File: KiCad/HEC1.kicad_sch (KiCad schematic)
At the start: 9 parts, among them J1 Barrel_Jack_Switch

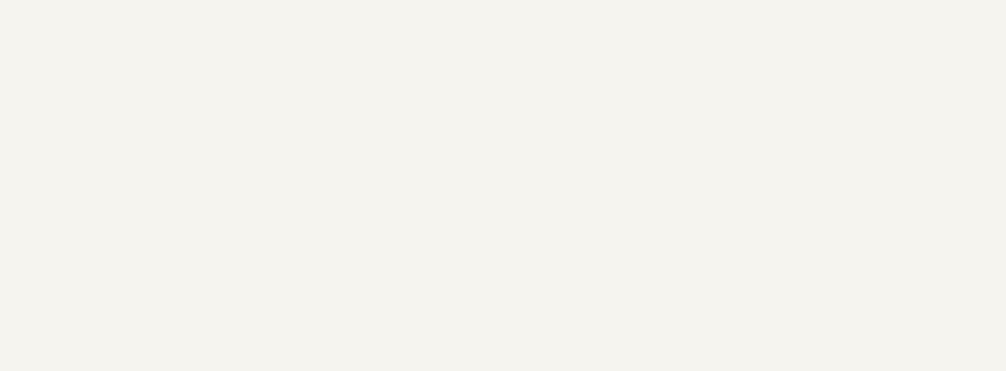
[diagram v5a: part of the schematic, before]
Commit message: MATX-compliant motherboard
Made the motherboard mounting holes and card positions MATX compliant. The MATX motherboard edge is shifted 0.5 inches to the left, which is annoying. Also, cards have component on the opposite side from ISA, meaning PCI slot positioning must be followed. However, PCI pins are not 0.1inch apart, so lining up is tricky. I don't know whether I got it right.
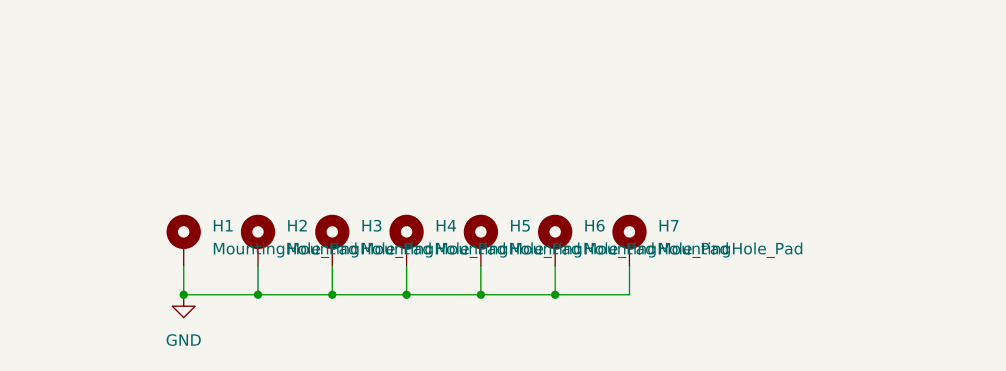
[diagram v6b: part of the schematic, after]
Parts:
- added H1, H2, H3, H4, H5, H6, H7: MountingHole_Pad, MountingHole:MountingHole_3.2mm_M3_Pad_Via, symbol Mechanical:MountingHole_Pad
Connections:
- net GND: now also H1.1, H2.1, H3.1, H4.1, H5.1, H6.1, H7.1

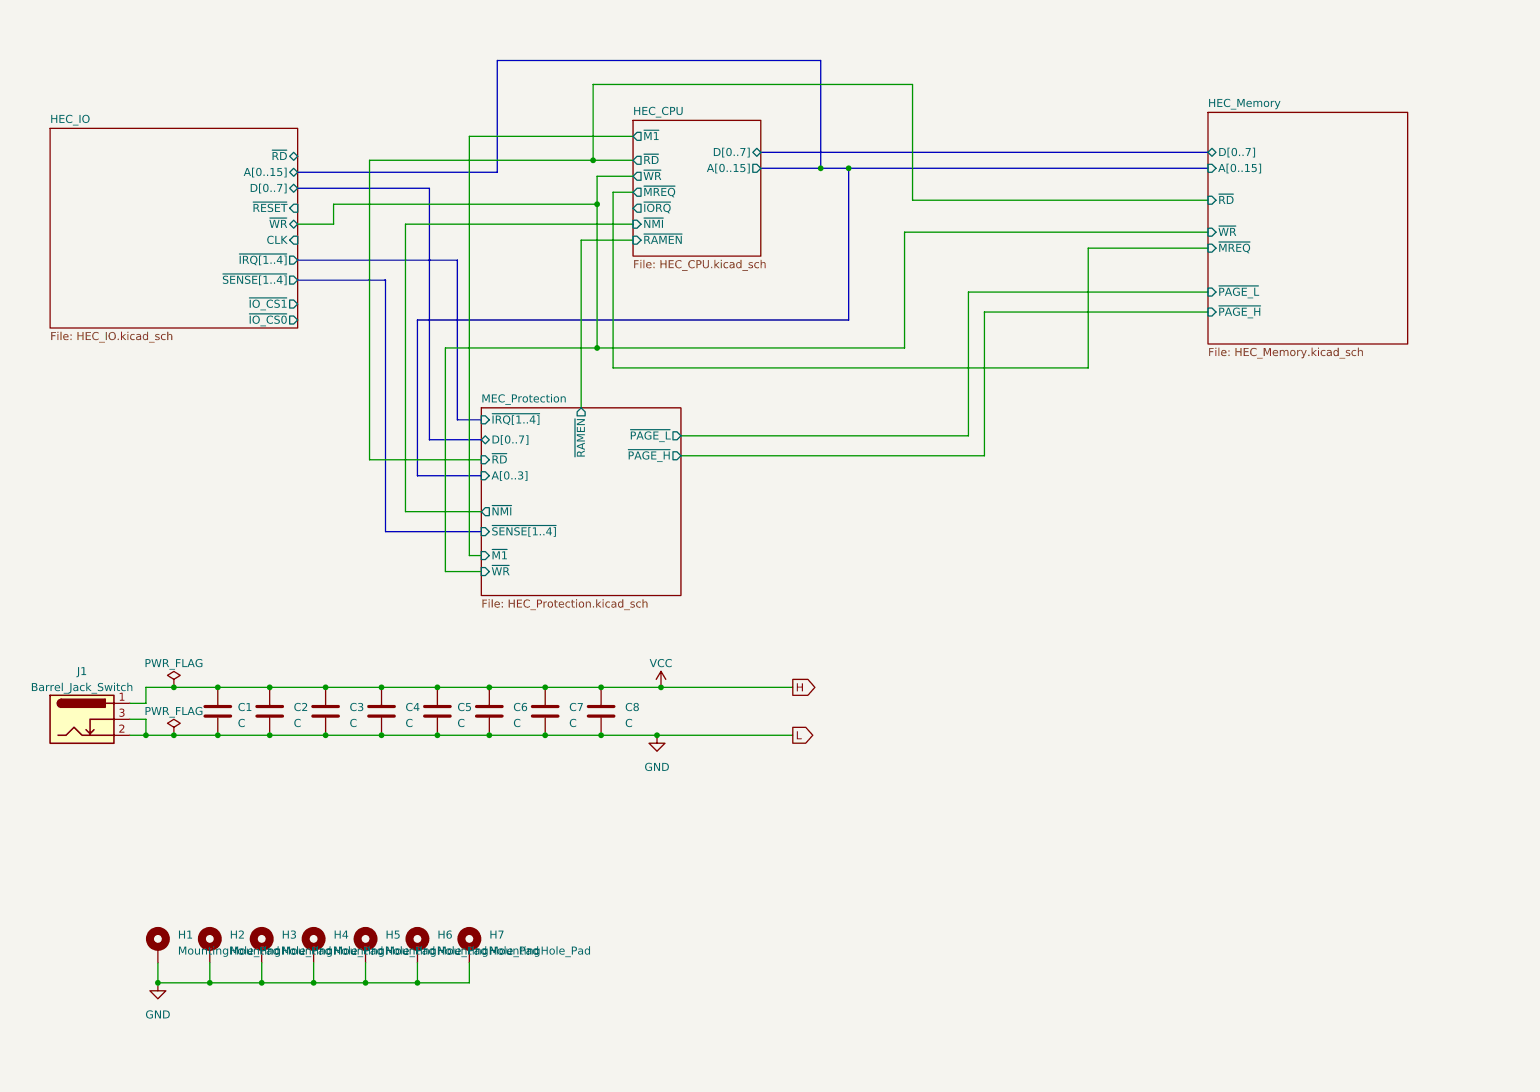
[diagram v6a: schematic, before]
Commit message: PCB Update
Some part placement, some routing, some change in schematic for easier PCB routing.
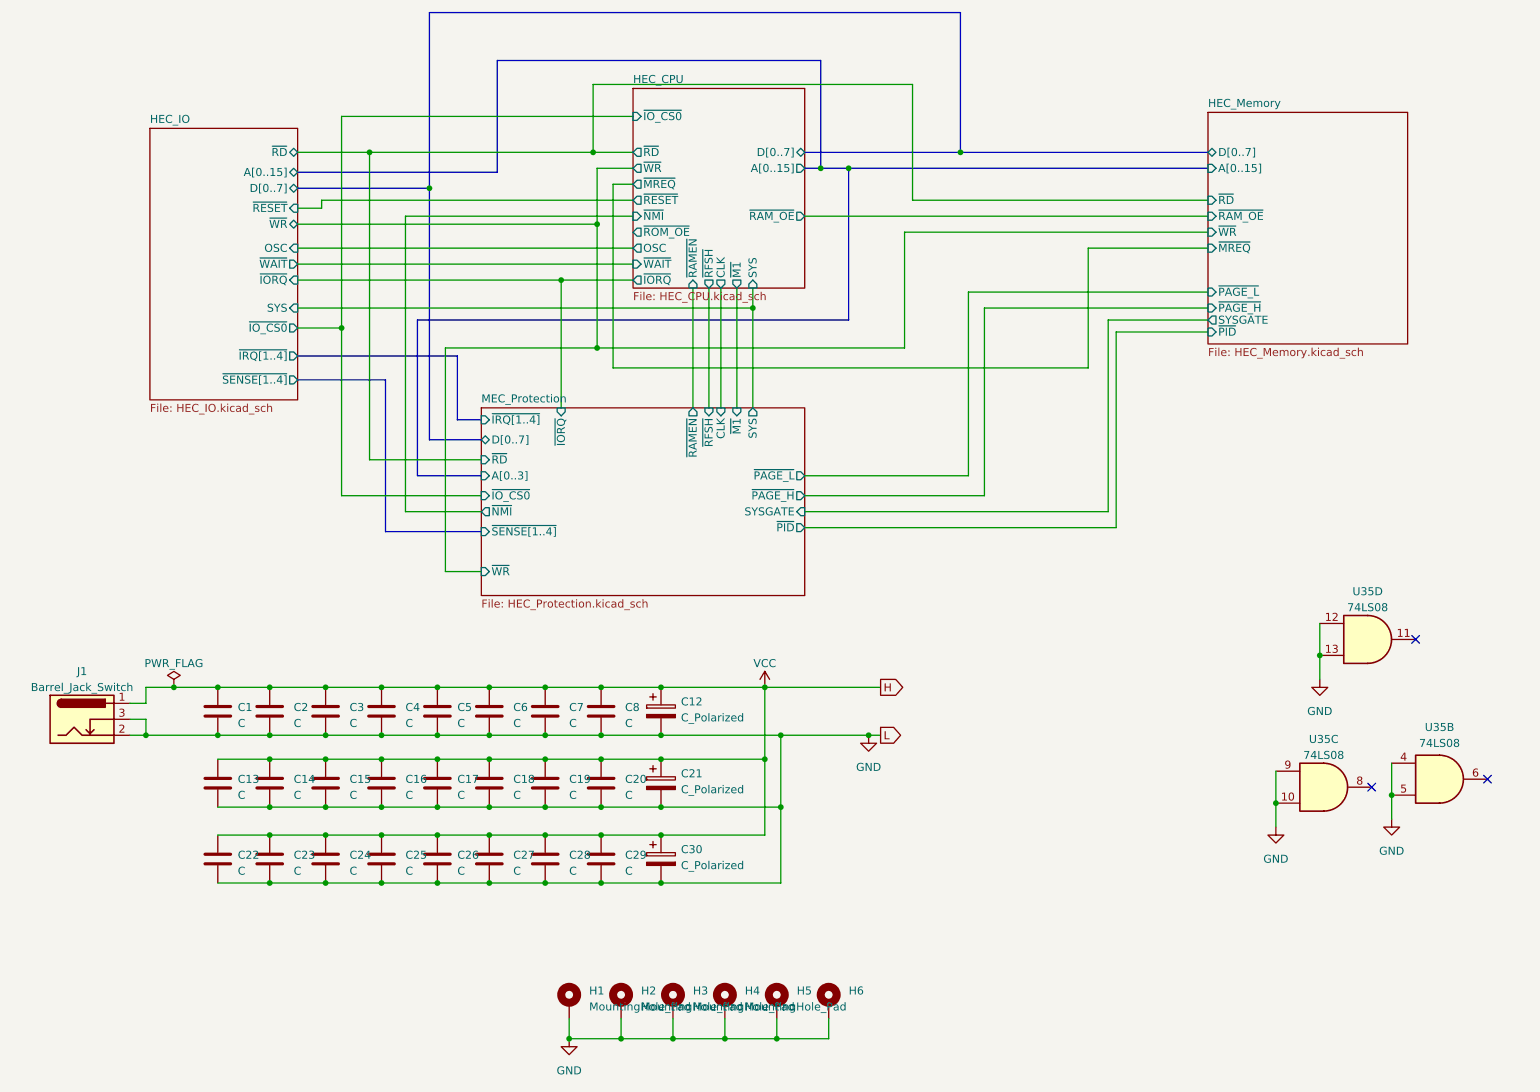
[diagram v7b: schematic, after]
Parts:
- removed H7: MountingHole_Pad, MountingHole:MountingHole_3.2mm_M3_Pad_Via, symbol Mechanical:MountingHole_Pad
- added C12, C21, C30: C_Polarized, Capacitor_THT:CP_Radial_D10.0mm_P5.00mm, symbol Device:C_Polarized
- added C13, C14, C15, C16, C17, C18, C19, C20, C22, C23, C24, C25, C26, C27, C28, C29: C, Capacitor_THT:C_Disc_D7.0mm_W2.5mm_P5.00mm, symbol Device:C
- added U35: 74LS08, Package_DIP:DIP-14_W7.62mm_Socket, symbol 74xx:74LS08
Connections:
- net GND: now also C12.2, C13.2, C14.2, C15.2, C16.2, C17.2, C18.2, C19.2, C20.2, C21.2, C22.2, C23.2, C24.2, C25.2, C26.2, C27.2, C28.2, C29.2, C30.2, U35.10, U35.12, U35.13, U35.4, U35.5, U35.9
- net VCC: now also C12.1, C13.1, C14.1, C15.1, C16.1, C17.1, C18.1, C19.1, C20.1, C21.1, C22.1, C23.1, C24.1, C25.1, C26.1, C27.1, C28.1, C29.1, C30.1
- no-connect marks 0 -> 3
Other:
- sheet HEC_CPU ports: added CLK, OSC, SYS, ~{IO_CS0}, ~{RAM_OE}, ~{RESET}, ~{RFSH}, ~{ROM_OE}, ~{WAIT}; removed none
- sheet HEC_IO ports: added OSC, SYS, ~{IORQ}, ~{WAIT}; removed CLK, ~{IO_CS1}
- sheet HEC_Memory ports: added SYSGATE, ~{PID}, ~{RAM_OE}; removed none
- sheet MEC_Protection ports: added CLK, SYS, SYSGATE, ~{IORQ}, ~{IO_CS0}, ~{PID}, ~{RFSH}; removed none
- moved on the sheet: H1, H2, H3, H4, H5, H6

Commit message: Cleanup schematic
Cleanup the schematic for easier reading, reduce ERC errors.
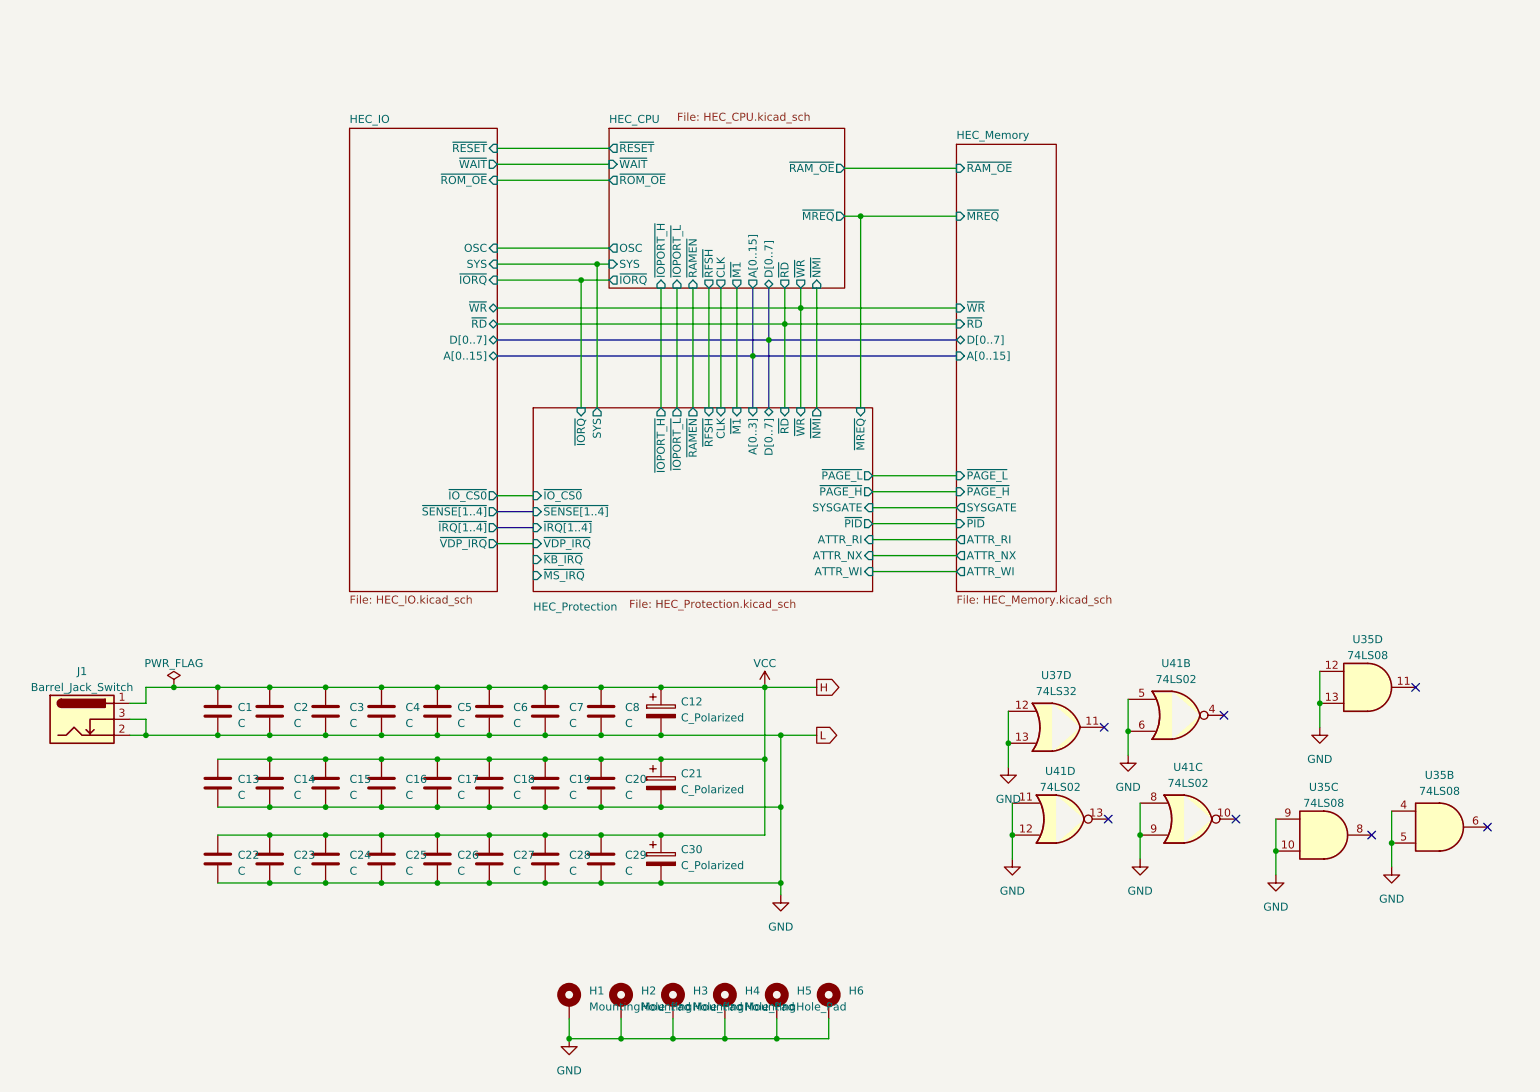
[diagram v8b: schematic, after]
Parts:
- added U37: 74LS32, Package_DIP:DIP-14_W7.62mm_Socket, symbol 74xx:74LS32
- added U41: 74LS02, symbol 74xx:74LS02
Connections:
- net GND: now also U37.12, U37.13, U41.11, U41.12, U41.5, U41.6, U41.8, U41.9
- no-connect marks 3 -> 7
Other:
- sheet MEC_Protection renamed HEC_Protection
- sheet HEC_CPU ports: added ~{IOPORT_H}, ~{IOPORT_L}; removed ~{IO_CS0}
- sheet HEC_IO ports: added ~{ROM_OE}, ~{VDP_IRQ}; removed none
- sheet HEC_Memory ports: added ATTR_NX, ATTR_RI, ATTR_WI; removed none
- sheet HEC_Protection ports: added ATTR_NX, ATTR_RI, ATTR_WI, ~{IOPORT_H}, ~{IOPORT_L}, ~{KB_IRQ}, ~{MREQ}, ~{MS_IRQ}, ~{VDP_IRQ}; removed none
- moved on the sheet: U35B, U35C, U35D
